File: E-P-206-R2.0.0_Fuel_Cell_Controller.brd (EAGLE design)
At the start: 160 x 100 mm, 175 parts

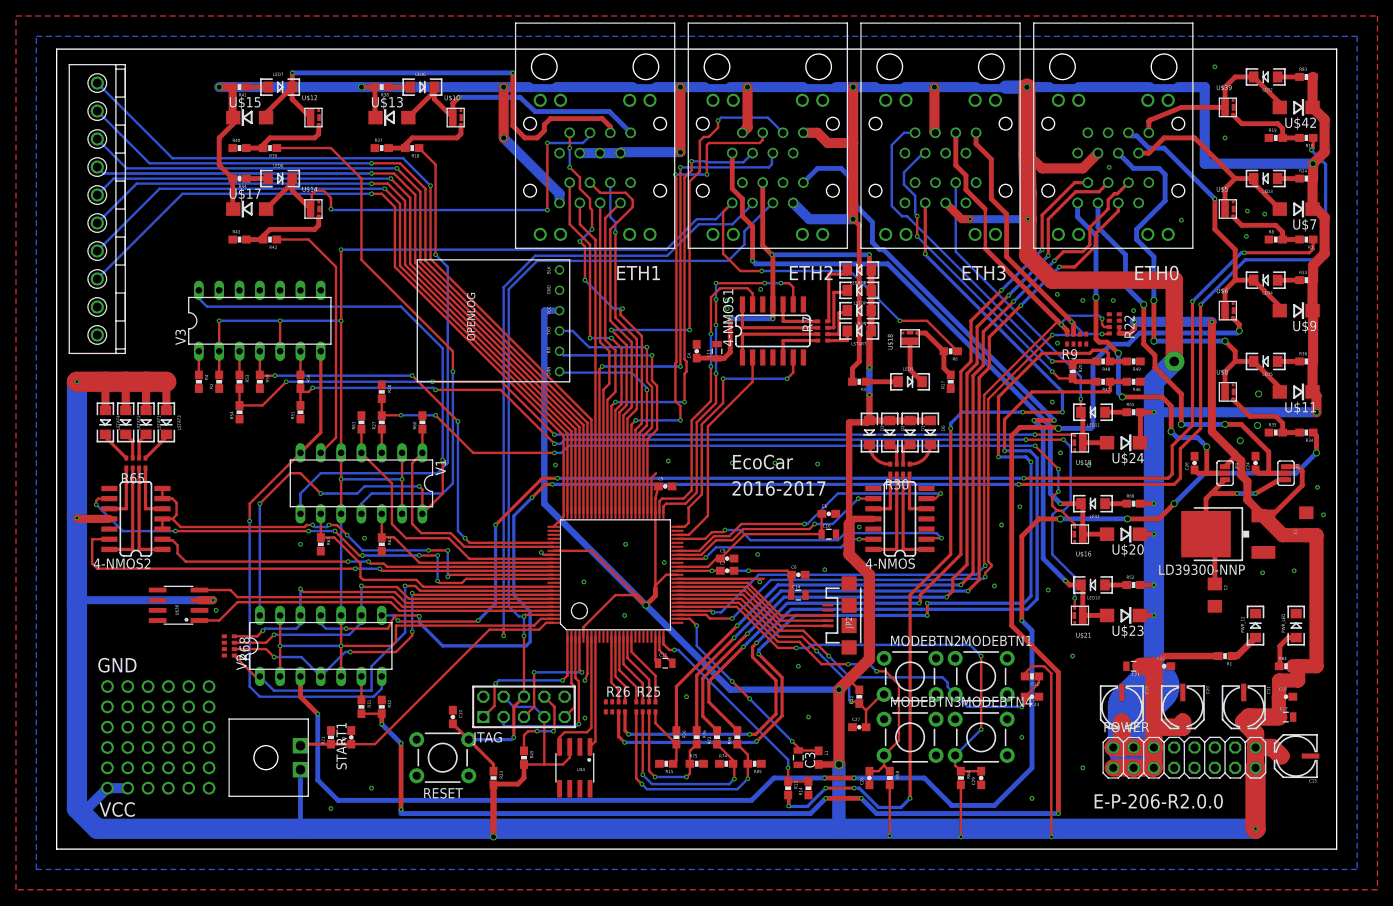
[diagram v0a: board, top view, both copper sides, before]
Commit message: Added some silkscreening and updated the relay board connection
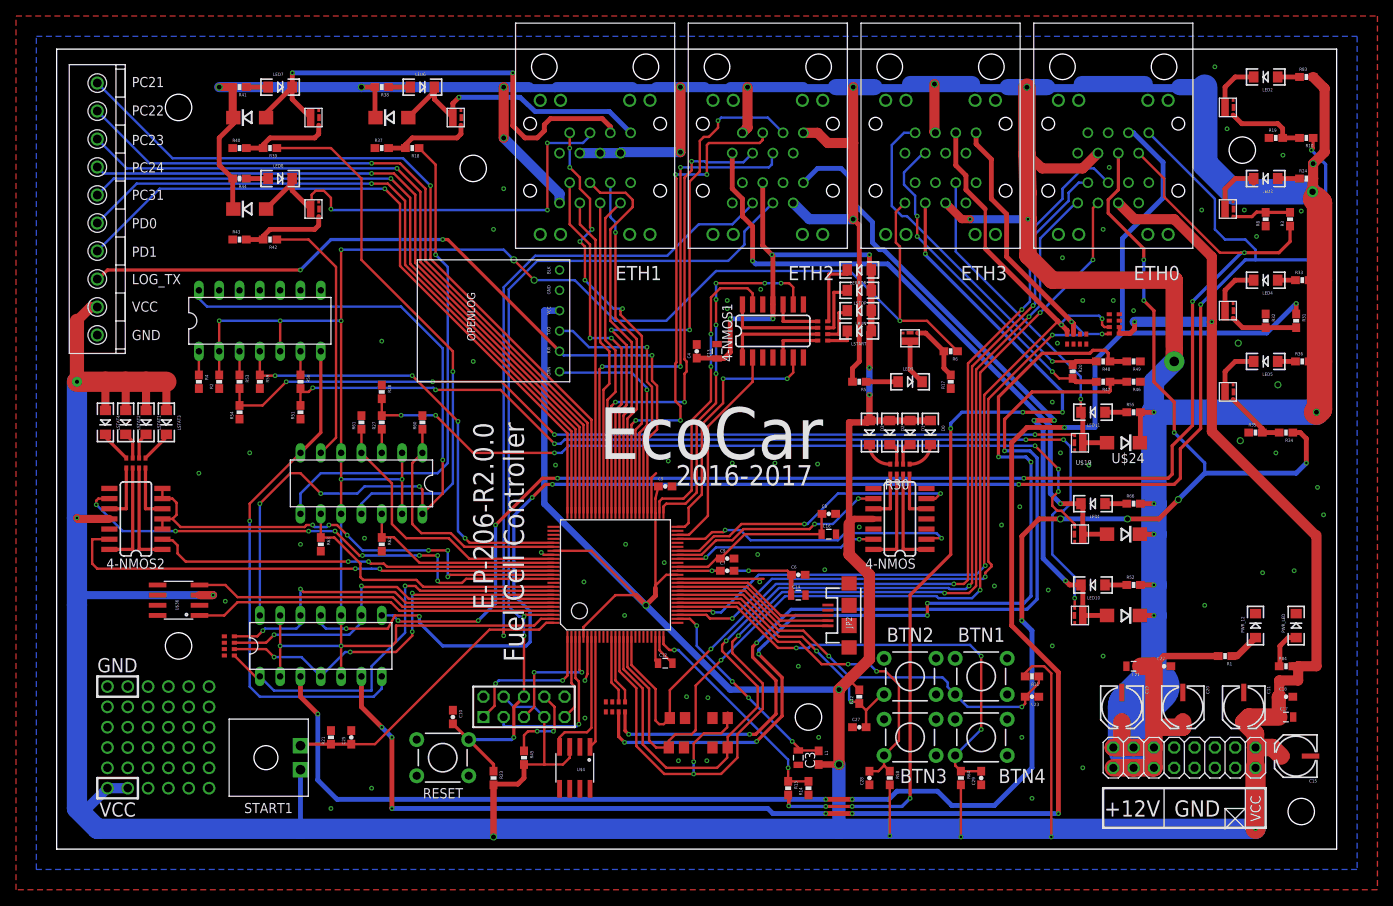
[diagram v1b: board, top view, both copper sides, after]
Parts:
- removed C1, C2: NNP, SparkFun:1206
- removed C24, C26: 100nF, SparkFun:0603-CAP
- removed JP1, JP4: JUMPER-31-2, SparkFun:SJ_3_PASTE1&2
- removed LD39300-NNP: LD117ADT50TR, v-reg:DPACK
- removed R25: 10k, SparkFun-Resistors:0603-ARV
- removed R73, R86: 31.6k 1%, SparkFun:0603-RES
- removed R74, R76, R85: 47k 1%, SparkFun:0603-RES
- removed R75: 3k 1%, SparkFun:0603-RES
- removed U$11, U$42, U$7, U$9: (no value), diode:DO214AC
- added R29, R56: 1M, resistor:R0805
- added U$22, U$25, U$26, U$27, U$28, U$3: (no value), SparkFun-Electromechanical:STAND-OFF
- R15: value 3k 1% -> 1M; device SparkFun:0603-RES -> resistor:R0805
- R16: value 47k 1% -> 1M; device SparkFun:0603-RES -> resistor:R0805
- moved R31 126.4 mm to (154.9, 66.0)
- moved R32 120.6 mm to (151.1, 66.0)
- moved R15 8.83 mm to (82.9, 16.4)
- moved R16 5.61 mm to (82.9, 12.7), turned to 180 degrees
- moved R3 3.25 mm to (154.2, 78.7), turned to 90 degrees
- moved R8 2.84 mm to (151.1, 78.7), turned to 90 degrees
- moved R34 2.54 mm to (153.7, 52.1)
- moved R35 2.54 mm to (149.9, 52.1)
- moved U$36 0.63 mm to (17.8, 28.6)
- moved R33 0.51 mm to (155.7, 71.1)
- moved R36 0.51 mm to (155.7, 61.0)
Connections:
- removed net 3V: C2.1, JP1.3, JP4.3, LD39300-NNP.4
- removed net CAPCURR: R86.2, RJ45_0_.T_2
- removed net CAPCURR_V_R: C26.1, JP4.2, RJ45_0_.T_1
- removed net CAPVOLT_R: R76.1, RJ45_0_.T_5
- removed net FCCURR: R73.2, RJ45_0_.T_4
- removed net FCCURR_V_R: C24.1, JP1.2, RJ45_0_.T_3
- removed net FCVOLT_R: R16.1, RJ45_0_.T_6
- removed net N$21: MCU.14, R25.4
- removed net N$27: MCU.15, R25.3
- removed net N$28: MCU.16, R25.2
- removed net N$29: MCU.17, R25.1
- removed net N$38: MCU.76, U$2.8
- new net FCC_R: RJ45_0_.T_6
- net +12V: no longer U$11.C, U$42.C, U$7.C, U$9.C
- net CAPCURR(S): now also MCU.14, R15.1, RJ45_0_.T_1; no longer R25.5, R85.2, R86.1
- net CAPREL_R: no longer RJ45_0_.B_3, U$9.A
- net CAPVOLT: now also MCU.16, R29.1, RJ45_0_.T_3; no longer R25.7, R75.1, R76.2
- net FCCURR(S): now also MCU.15, R16.1, RJ45_0_.T_2; no longer R25.6, R73.1, R74.2
- net FCVOLT: now also MCU.17, R56.1, RJ45_0_.T_4; no longer R15.1, R16.2, R25.8
- net GND: now also R16.2, R29.2, R56.2, RJ45_0_.B_7, RJ45_0_.B_8, U$2.10; no longer C1.2, C2.2, C24.2, C26.2, LD39300-NNP.1, R74.1, R75.2, R85.1, RJ45_3_.T_1
- net MOTORREL_R: no longer RJ45_0_.B_2, U$7.A
- net OP-1S: now also RJ45_0_.B_1
- net OP-2S: now also RJ45_0_.B_2
- net OP-3S: now also RJ45_0_.B_3
- net OP-4S: now also RJ45_0_.B_4
- net OPENLOG_TX: now also U$2.8
- net RESREL_R: no longer RJ45_0_.B_4, U$11.A
- net STARTUPREL_R: no longer RJ45_0_.B_1, U$42.A
- net SYS_OK: now also RJ45_3_.T_1; no longer RJ45_2_.T_1
- net VCC: now also RJ45_0_.T_5, U$2.9; no longer C1.1, JP1.1, JP4.1, LD39300-NNP.3
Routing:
- net OP-3S: track 2.96 -> 228.7 mm, vias 0 -> 8
- net N$20: track 190.0 -> 8.36 mm, vias 8 -> 0
- net CAPCURR(S): track 28.2 -> 144.3 mm, vias 2 -> 5
- net FCVOLT: track 7.74 -> 121.8 mm, vias 0 -> 3
- net FCCURR(S): track 25.3 -> 135.5 mm, vias 2 -> 3
- net FCVOLT_R: track 106.9 -> 0.00 mm, vias 4 -> 0
- net CAPVOLT: track 17.0 -> 122.4 mm, vias 2 -> 4
- net FCCURR: track 103.8 -> 0.00 mm, vias 4 -> 0
- net CAPVOLT_R: track 102.6 -> 0.00 mm, vias 4 -> 0
- net CAPCURR: track 100.2 -> 0.00 mm, vias 4 -> 0
- net N$38: track 91.5 -> 0.00 mm, vias 1 -> 0
- net OPENLOG_TX: track 32.2 -> 97.8 mm, vias 1 -> 3
- net FCCURR_V_R: track 51.0 -> 0.00 mm, vias 3 -> 0
- net CAPCURR_V_R: track 49.4 -> 0.00 mm, vias 5 -> 0
- net RESREL_R: track 53.9 -> 6.65 mm, vias 3 -> 0
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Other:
- board text added: "+12V"
- board text added: "BTN1"
- board text added: "BTN2"
- board text added: "BTN3"
- board text added: "BTN4"
- board text added: "Fuel Cell Controller"
- board text added: "LOG_TX"
- board text added: "PC21"
- board text added: "PC22"
- board text added: "PC23"
- board text added: "PC24"
- board text added: "PC31"
- board text added: "PD0"
- board text added: "PD1"
